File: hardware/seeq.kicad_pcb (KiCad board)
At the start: 2 copper layers, 199.5 x 82 mm, 88 parts, among them J1 MIDI IN, J2 AudioJack2_SwitchT, J3 Conn_01x06, J4 Conn_01x04, J5 AudioJack2_SwitchT, J6 MIDI OUT, SW1 SW_DIP_x01, SW10 SW_DIP_x01, SW11 SW_DIP_x01, SW12 SW_DIP_x01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

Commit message: Update software for PCB + PCB fixes
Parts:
- D34, D35, D36, D37: value WS2812 -> WS2812B; footprint LED_SMD:LED_WS2812_PLCC6_5.0x5.0mm_P1.6mm -> LED_SMD:LED_WS2812B_PLCC4_5.0x5.0mm_P3.2mm
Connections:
- D34 pad 1: Net-(D34-Pad1) -> +3V3
- D34 pad 2: LED -> Net-(D34-Pad2)
- D34 pad 3: +5V -> GND
- D34 pad 4: unconnected-(D34-Pad4) -> LED
- D35 pad 1: Net-(D35-Pad1) -> +3V3
- D35 pad 2: Net-(D34-Pad1) -> Net-(D35-Pad2)
- D35 pad 3: +5V -> GND
- D35 pad 4: unconnected-(D35-Pad4) -> Net-(D34-Pad2)
- D36 pad 1: Net-(D36-Pad1) -> +3V3
- D36 pad 2: Net-(D35-Pad1) -> Net-(D36-Pad2)
- D36 pad 3: +5V -> GND
- D36 pad 4: unconnected-(D36-Pad4) -> Net-(D35-Pad2)
- D37 pad 1: unconnected-(D37-Pad1) -> +3V3
- D37 pad 2: Net-(D36-Pad1) -> unconnected-(D37-Pad2)
- D37 pad 3: +5V -> GND
- D37 pad 4: unconnected-(D37-Pad4) -> Net-(D36-Pad2)
- U2 pad 26: SCL -> SDA
- U2 pad 27: SDA -> SCL
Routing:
- net +5V: track 266.6 -> 87.6 mm, vias 1 -> 0
- net Net-(D35-Pad1): track 61.7 -> 0.00 mm
- net Net-(D36-Pad1): track 61.1 -> 0.00 mm
- net Net-(D35-Pad2): track 0.00 -> 55.5 mm
- net Net-(D36-Pad2): track 0.00 -> 54.9 mm
- net Net-(D34-Pad1): track 37.0 -> 0.00 mm
- net Net-(D34-Pad2): track 0.00 -> 30.8 mm
- net LED: track 45.1 -> 40.2 mm, vias 2 -> 0
- net SCL: track 38.2 -> 35.6 mm
- net SDA: track 38.0 -> 40.5 mm
- net +3V3: track 265.4 -> 263.4 mm

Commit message: Add kibot and docs
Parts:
- removed the G*** at (148.6, 105.8)
- added C1: 1uF, Capacitor_THT:C_Disc_D5.0mm_W2.5mm_P5.00mm, F.Cu at (198.2, 95.9)
- added D38: WS2812B, LED_SMD:LED_WS2812B_PLCC4_5.0x5.0mm_P3.2mm, B.Cu at (127.8, 103.0)
- added D39: WS2812B, LED_SMD:LED_WS2812B_PLCC4_5.0x5.0mm_P3.2mm, B.Cu at (111.8, 102.9)
- added D40: WS2812B, LED_SMD:LED_WS2812B_PLCC4_5.0x5.0mm_P3.2mm, B.Cu at (95.8, 102.9)
- added D41: WS2812B, LED_SMD:LED_WS2812B_PLCC4_5.0x5.0mm_P3.2mm, B.Cu at (79.8, 102.9)
- added D42: WS2812B, LED_SMD:LED_WS2812B_PLCC4_5.0x5.0mm_P3.2mm, B.Cu at (63.8, 102.9)
- added D43: WS2812B, LED_SMD:LED_WS2812B_PLCC4_5.0x5.0mm_P3.2mm, B.Cu at (47.8, 102.9)
- added G***: LOGO, mod:notes, F.Cu at (16.5, 66.7)
- added G***: LOGO, mod:logo, F.Cu at (58.2, 66.5)
- added G***: LOGO, mod:notes, B.Cu at (49.3, 66.6)
- added G***: LOGO, mod:logo-big, B.Cu at (128.7, 74.7)
- J2, J5: value AudioJack2_SwitchT -> AudioJack2; footprint Connector_Audio:Jack_3.5mm_CUI_SJ1-3533NG_Horizontal_CircularHoles -> Keebio-Parts:TRRS-PJ-320A-no-Fmask
- moved D37 98.7 mm to (143.8, 103.0)
- moved D36 56.3 mm to (159.8, 103.0)
- moved D9 27.8 mm to (84.2, 65.4)
- moved D35 13.4 mm to (175.8, 103.0)
- moved D10 6.11 mm to (84.2, 62.5)
- moved J2 5.77 mm to (133.1, 26.0)
- moved J5 5.76 mm to (113.9, 26.0)
- moved D34 5.47 mm to (191.8, 103.0)
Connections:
- D34 pad 1: +3V3 -> +5V
- D35 pad 1: +3V3 -> +5V
- D36 pad 1: +3V3 -> +5V
- D37 pad 1: +3V3 -> +5V
- D37 pad 2: unconnected-(D37-Pad2) -> Net-(D37-Pad2)
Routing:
- net +5V: track 87.6 -> 271.6 mm
- net +3V3: track 263.4 -> 80.3 mm
- net Net-(D35-Pad2): track 55.5 -> 12.5 mm
- net Net-(D36-Pad2): track 54.9 -> 12.5 mm
- net Net-(D9-Pad2): track 17.9 -> 46.7 mm, vias 0 -> 1
- net Net-(D10-Pad1): track 177.4 -> 151.6 mm
- net Net-(D34-Pad2): track 30.8 -> 12.5 mm
- net Net-(D37-Pad2): track 0.00 -> 12.5 mm
- net Net-(D40-Pad2): track 0.00 -> 12.5 mm
- net Net-(D39-Pad2): track 0.00 -> 12.5 mm
- net Net-(D42-Pad2): track 0.00 -> 12.5 mm
- net Net-(D41-Pad2): track 0.00 -> 12.5 mm
- net Net-(D39-Pad4): track 0.00 -> 12.4 mm
- net Net-(J5-PadS): track 122.7 -> 116.2 mm
- net LED: track 40.2 -> 44.9 mm
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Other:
- board text added: "${VERSION}"
- board text added: "MIDI and CV/Gate Sequencer"
- board text added: "https://6px.eu/seeq"

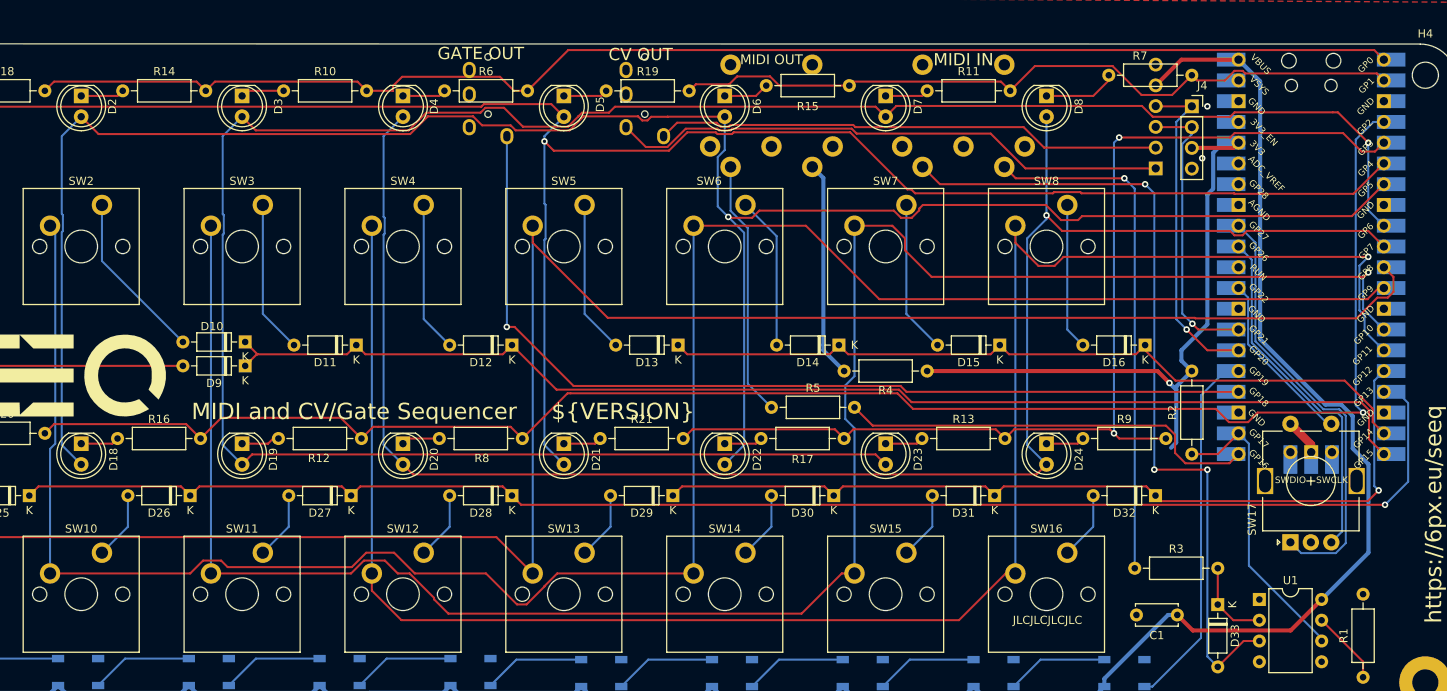
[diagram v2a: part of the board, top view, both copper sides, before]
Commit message: fix erc / drc
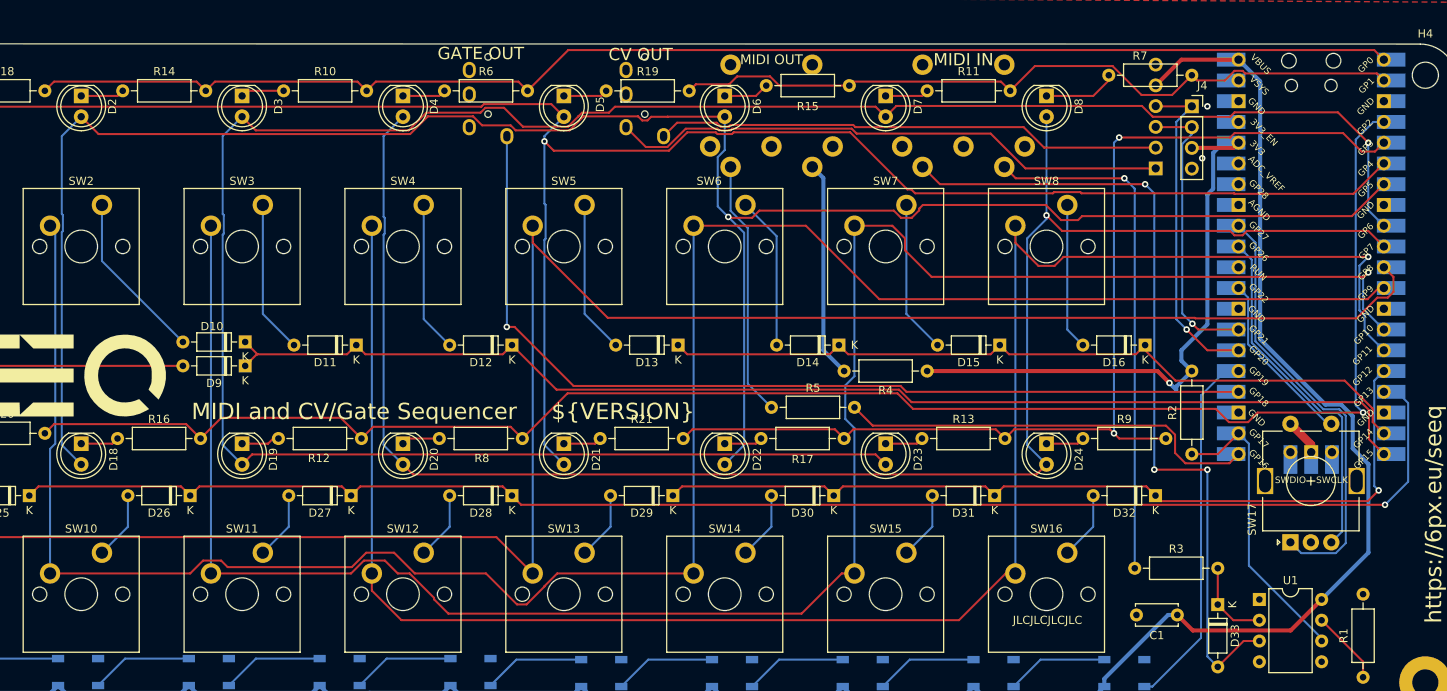
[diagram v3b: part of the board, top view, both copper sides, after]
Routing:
- net +3V3: track 80.3 -> 71.1 mm
- net LED: track 44.9 -> 43.3 mm
- net Net-(D25-Pad1): track 186.3 -> 184.7 mm
- net Net-(SW10-Pad2): track 259.0 -> 257.5 mm
- net Net-(D29-Pad1): track 105.3 -> 104.3 mm
- net Net-(D3-Pad1): track 5.34 -> 4.45 mm
- net Net-(D20-Pad1): track 4.71 -> 3.81 mm
- net Net-(R10-Pad2): track 170.0 -> 169.2 mm
- net Net-(D13-Pad1): track 95.0 -> 94.3 mm
- net Net-(D10-Pad1): track 151.6 -> 151.0 mm
